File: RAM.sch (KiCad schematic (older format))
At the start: 19 parts, among them U1 xc7a50tftg256, U14 W9751G6KB

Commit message: using BOMs AWAY to create BOM
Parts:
- C126, C129: MFR (none) -> Murata; MPN (none) -> GRM21BR61A106KE19L
- C127, C128, C130, C131, C132, C133: MFR (none) -> Murata; MPN (none) -> GRM188R71C104KA01D
- C136: MFR (none) -> Murata Manufacturing Co Ltd; MPN (none) -> GRM32ER70J476ME20L
- C137, C138: MFR (none) -> Murata; MPN (none) -> GRM21BR61A475KA73L
- C139, C140, C141, C142: MFR (none) -> Murata; MPN (none) -> GRM188R71C474KA88D
- R56, R57: MFR (none) -> Vishay Dale; MPN (none) -> CRCW040210K0FKED
- U1: MFR (none) -> Xilinx; MPN (none) -> XC7A50T-1FTG256C
- U14: MFR (none) -> Winbond Electronics Corp; MPN (none) -> W9751G6KB-25

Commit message: just added NOTE field to BOMS AWAY
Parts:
- C126, C129: SPN (none) -> 490-1709-1-ND; SPR (none) -> Digikey
- C127, C128, C130, C131, C132, C133: SPN (none) -> 490-1532-1-ND; SPR (none) -> Digikey
- C136: SPN (none) -> 490-6542-1-ND; SPR (none) -> Digikey
- C137, C138: SPN (none) -> 490-9750-1-ND; SPR (none) -> Digikey
- C139, C140, C141, C142: SPN (none) -> 490-3295-1-ND; SPR (none) -> Digikey
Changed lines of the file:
@@
 F 4 "Murata" H 0 0 50 0001 C CNN "MFR"
 F 5 "GRM188R71C104KA01D" H 0 0 50 0001 C CNN "MPN"
-F 6 "" H 0 0 50 0001 C CNN "SPR"
-F 7 "" H 0 0 50 0001 C CNN "SPN"
+F 6 "Digikey" H 0 0 50 0001 C CNN "SPR"
+F 7 "490-1532-1-ND" H 0 0 50 0001 C CNN "SPN"
 F 8 "" H 0 0 50 0001 C CNN "SPURL"
 	1    1000 4550
@@
 F 4 "Murata" H 0 0 50 0001 C CNN "MFR"
 F 5 "GRM188R71C104KA01D" H 0 0 50 0001 C CNN "MPN"
-F 6 "" H 0 0 50 0001 C CNN "SPR"
-F 7 "" H 0 0 50 0001 C CNN "SPN"
+F 6 "Digikey" H 0 0 50 0001 C CNN "SPR"
+F 7 "490-1532-1-ND" H 0 0 50 0001 C CNN "SPN"
 F 8 "" H 0 0 50 0001 C CNN "SPURL"
 	1    1000 5050
@@
 F 4 "Murata" H 0 0 50 0001 C CNN "MFR"
 F 5 "GRM188R71C104KA01D" H 0 0 50 0001 C CNN "MPN"
-F 6 "" H 0 0 50 0001 C CNN "SPR"
-F 7 "" H 0 0 50 0001 C CNN "SPN"
+F 6 "Digikey" H 0 0 50 0001 C CNN "SPR"
+F 7 "490-1532-1-ND" H 0 0 50 0001 C CNN "SPN"
 F 8 "" H 0 0 50 0001 C CNN "SPURL"
 	1    1600 4550
@@
 F 4 "Murata" H 0 0 50 0001 C CNN "MFR"
 F 5 "GRM188R71C104KA01D" H 0 0 50 0001 C CNN "MPN"
-F 6 "" H 0 0 50 0001 C CNN "SPR"
-F 7 "" H 0 0 50 0001 C CNN "SPN"
+F 6 "Digikey" H 0 0 50 0001 C CNN "SPR"
+F 7 "490-1532-1-ND" H 0 0 50 0001 C CNN "SPN"
 F 8 "" H 0 0 50 0001 C CNN "SPURL"
 	1    1600 5050
@@
 F 4 "Murata" H 0 0 50 0001 C CNN "MFR"
 F 5 "GRM188R71C104KA01D" H 0 0 50 0001 C CNN "MPN"
-F 6 "" H 0 0 50 0001 C CNN "SPR"
-F 7 "" H 0 0 50 0001 C CNN "SPN"
+F 6 "Digikey" H 0 0 50 0001 C CNN "SPR"
+F 7 "490-1532-1-ND" H 0 0 50 0001 C CNN "SPN"
 F 8 "" H 0 0 50 0001 C CNN "SPURL"
 	1    1500 6000
@@
 F 4 "Murata" H 0 0 50 0001 C CNN "MFR"
 F 5 "GRM188R71C104KA01D" H 0 0 50 0001 C CNN "MPN"
-F 6 "" H 0 0 50 0001 C CNN "SPR"
-F 7 "" H 0 0 50 0001 C CNN "SPN"
+F 6 "Digikey" H 0 0 50 0001 C CNN "SPR"
+F 7 "490-1532-1-ND" H 0 0 50 0001 C CNN "SPN"
 F 8 "" H 0 0 50 0001 C CNN "SPURL"
 	1    1250 6000
@@
 F 4 "Murata" H 0 0 50 0001 C CNN "MFR"
 F 5 "GRM21BR61A106KE19L" H 0 0 50 0001 C CNN "MPN"
-F 6 "" H 0 0 50 0001 C CNN "SPR"
-F 7 "" H 0 0 50 0001 C CNN "SPN"
+F 6 "Digikey" H 0 0 50 0001 C CNN "SPR"
+F 7 "490-1709-1-ND" H 0 0 50 0001 C CNN "SPN"
 F 8 "" H 0 0 50 0001 C CNN "SPURL"
 	1    1000 6000
@@
 F 4 "Murata" H 0 0 50 0001 C CNN "MFR"
 F 5 "GRM21BR61A106KE19L" H 0 0 50 0001 C CNN "MPN"
-F 6 "" H 0 0 50 0001 C CNN "SPR"
-F 7 "" H 0 0 50 0001 C CNN "SPN"
+F 6 "Digikey" H 0 0 50 0001 C CNN "SPR"
+F 7 "490-1709-1-ND" H 0 0 50 0001 C CNN "SPN"
 F 8 "" H 0 0 50 0001 C CNN "SPURL"
 	1    750  6000
@@
 F 4 "Murata Manufacturing Co Ltd" H 0 0 50 0001 C CNN "MFR"
 F 5 "GRM32ER70J476ME20L" H 0 0 50 0001 C CNN "MPN"
-F 6 "" H 0 0 50 0001 C CNN "SPR"
-F 7 "" H 0 0 50 0001 C CNN "SPN"
+F 6 "Digikey" H 0 0 50 0001 C CNN "SPR"
+F 7 "490-6542-1-ND" H 0 0 50 0001 C CNN "SPN"
 F 8 "" H 0 0 50 0001 C CNN "SPURL"
 	1    6900 5950
@@
 F 4 "Murata" H 0 0 50 0001 C CNN "MFR"
 F 5 "GRM21BR61A475KA73L" H 0 0 50 0001 C CNN "MPN"
-F 6 "" H 0 0 50 0001 C CNN "SPR"
-F 7 "" H 0 0 50 0001 C CNN "SPN"
+F 6 "Digikey" H 0 0 50 0001 C CNN "SPR"
+F 7 "490-9750-1-ND" H 0 0 50 0001 C CNN "SPN"
 F 8 "" H 0 0 50 0001 C CNN "SPURL"
 	1    7150 5950
@@
 F 4 "Murata" H 0 0 50 0001 C CNN "MFR"
 F 5 "GRM21BR61A475KA73L" H 0 0 50 0001 C CNN "MPN"
-F 6 "" H 0 0 50 0001 C CNN "SPR"
-F 7 "" H 0 0 50 0001 C CNN "SPN"
+F 6 "Digikey" H 0 0 50 0001 C CNN "SPR"
+F 7 "490-9750-1-ND" H 0 0 50 0001 C CNN "SPN"
 F 8 "" H 0 0 50 0001 C CNN "SPURL"
 	1    7400 5950
@@
 F 4 "Murata" H 0 0 50 0001 C CNN "MFR"
 F 5 "GRM188R71C474KA88D" H 0 0 50 0001 C CNN "MPN"
-F 6 "" H 0 0 50 0001 C CNN "SPR"
-F 7 "" H 0 0 50 0001 C CNN "SPN"
+F 6 "Digikey" H 0 0 50 0001 C CNN "SPR"
+F 7 "490-3295-1-ND" H 0 0 50 0001 C CNN "SPN"
 F 8 "" H 0 0 50 0001 C CNN "SPURL"
 	1    7650 5950
@@
 F 4 "Murata" H 0 0 50 0001 C CNN "MFR"
 F 5 "GRM188R71C474KA88D" H 0 0 50 0001 C CNN "MPN"
-F 6 "" H 0 0 50 0001 C CNN "SPR"
-F 7 "" H 0 0 50 0001 C CNN "SPN"
+F 6 "Digikey" H 0 0 50 0001 C CNN "SPR"
+F 7 "490-3295-1-ND" H 0 0 50 0001 C CNN "SPN"
 F 8 "" H 0 0 50 0001 C CNN "SPURL"
 	1    7900 5950
@@
 F 4 "Murata" H 0 0 50 0001 C CNN "MFR"
 F 5 "GRM188R71C474KA88D" H 0 0 50 0001 C CNN "MPN"
-F 6 "" H 0 0 50 0001 C CNN "SPR"
-F 7 "" H 0 0 50 0001 C CNN "SPN"
+F 6 "Digikey" H 0 0 50 0001 C CNN "SPR"
+F 7 "490-3295-1-ND" H 0 0 50 0001 C CNN "SPN"
 F 8 "" H 0 0 50 0001 C CNN "SPURL"
 	1    8150 5950
@@
 F 4 "Murata" H 0 0 50 0001 C CNN "MFR"
 F 5 "GRM188R71C474KA88D" H 0 0 50 0001 C CNN "MPN"
-F 6 "" H 0 0 50 0001 C CNN "SPR"
-F 7 "" H 0 0 50 0001 C CNN "SPN"
+F 6 "Digikey" H 0 0 50 0001 C CNN "SPR"
+F 7 "490-3295-1-ND" H 0 0 50 0001 C CNN "SPN"
 F 8 "" H 0 0 50 0001 C CNN "SPURL"
 	1    8400 5950

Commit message: Complete BOM. all resistors now 0402
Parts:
- R56, R57: MFR Vishay Dale -> Yageo; MPN CRCW040210K0FKED -> RC0402FR-0710KL; SPN (none) -> 311-10.0KLRTR-ND; SPR (none) -> Digikey
- U1: SPN (none) -> 122-1916-ND; SPR (none) -> Digikey
- U14: SPN (none) -> W9751G6KB-25-ND; SPR (none) -> Digikey

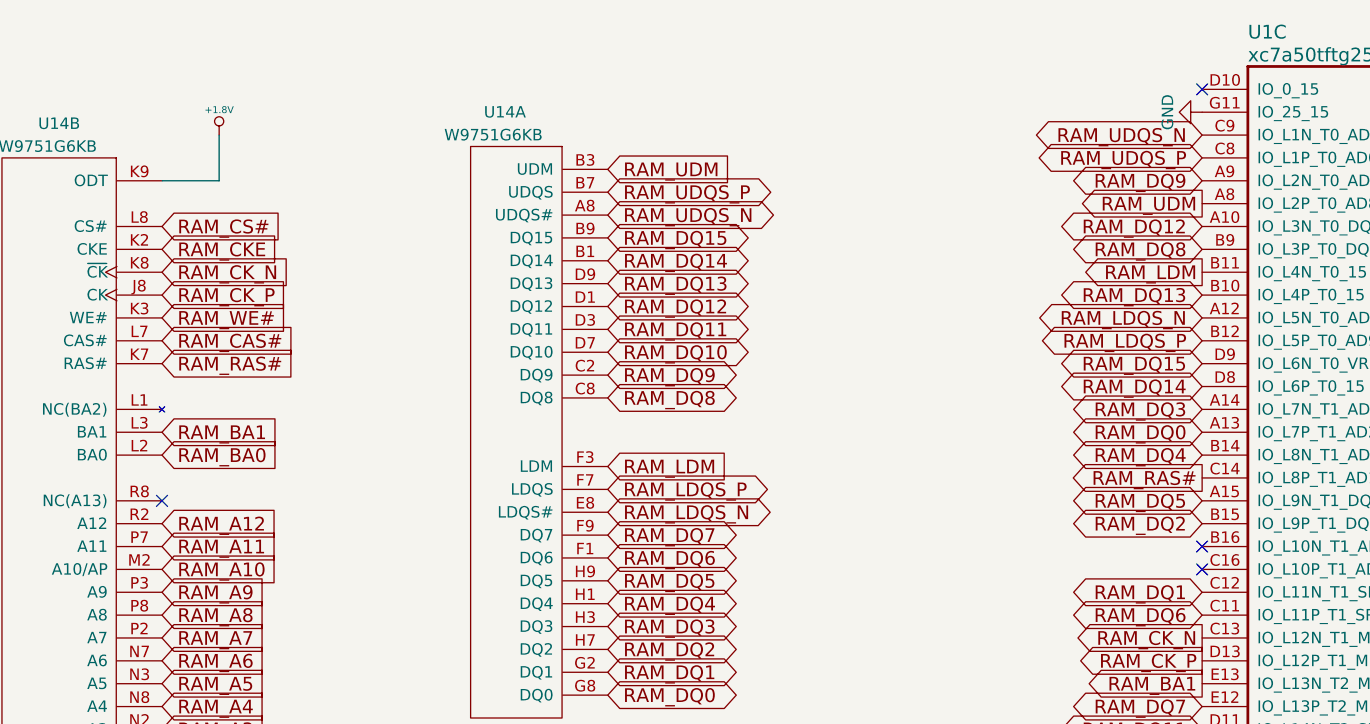
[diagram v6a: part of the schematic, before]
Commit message: attached RAM_ODT signal
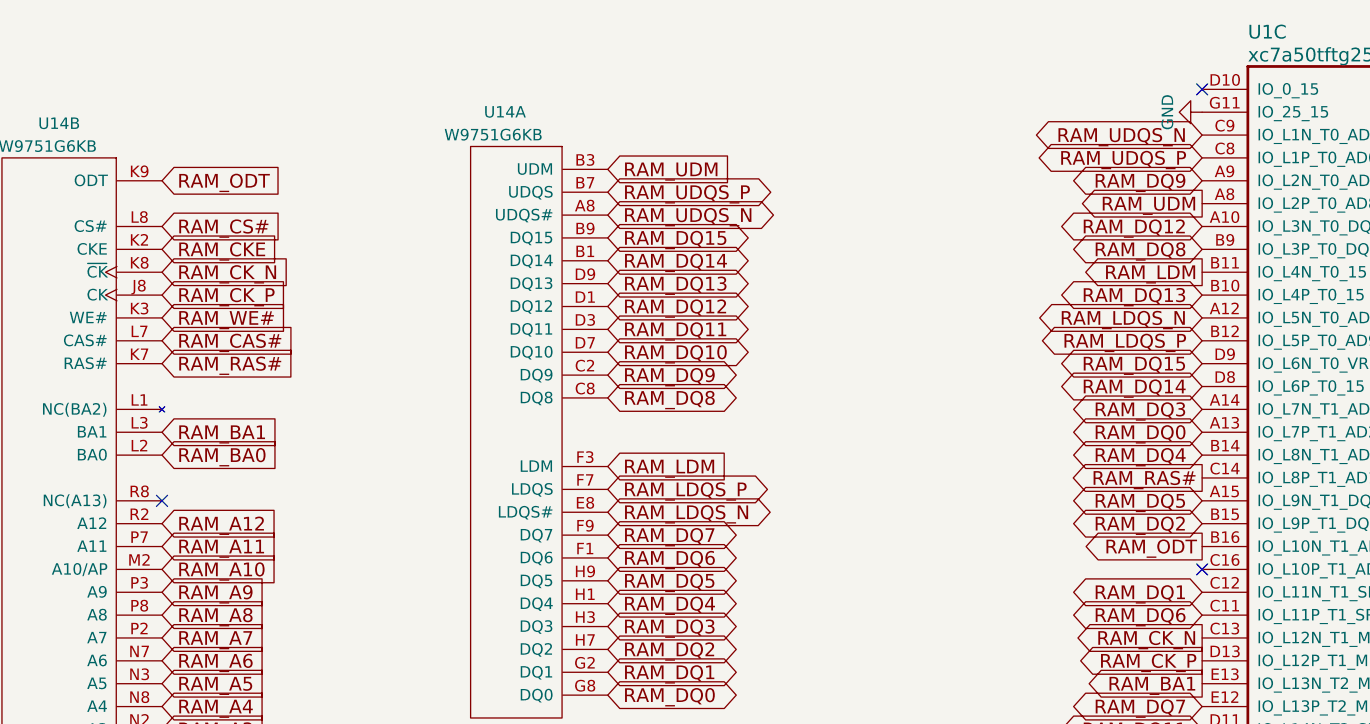
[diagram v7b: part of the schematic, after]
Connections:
- net +1.8V: no longer U14.K9 (ODT)
- net RAM_ODT: now reaches U1.B16 (IO_L10N_T1_AD11N_15)
- net RAM_ODT: now also U14.K9 (ODT)
- no-connect marks 6 -> 5
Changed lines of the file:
@@
-$EndComp
-$Comp
-L +1.8V #PWR0213
-U 1 1 58828F8D
-P 4850 1250
-F 0 "#PWR0213" H 4850 1390 20  0001 C CNN
-F 1 "+1.8V" H 4850 1360 30  0000 C CNN
-F 2 "" H 4850 1250 60  0001 C CNN
-F 3 "" H 4850 1250 60  0001 C CNN
-	1    4850 1250
-	1    0    0    -1
 $EndComp
 $Comp
@@
 	2250 6900 2050 6900
 Wire Wire Line
-	4850 1250 4850 1450
-Wire Wire Line
-	4850 1450 4600 1450
-Wire Wire Line
 	2050 7000 2050 5250
 Wire Wire Line
@@
 NoConn ~ 9150 4950
 NoConn ~ 4600 2850
-NoConn ~ 9150 3050
 NoConn ~ 9150 3150
 NoConn ~ 9150 1050
+Text GLabel 4600 1450 2    60   Input ~ 0
+RAM_ODT
+Text GLabel 9150 3050 0    60   Output ~ 0
+RAM_ODT
 $EndSCHEMATC

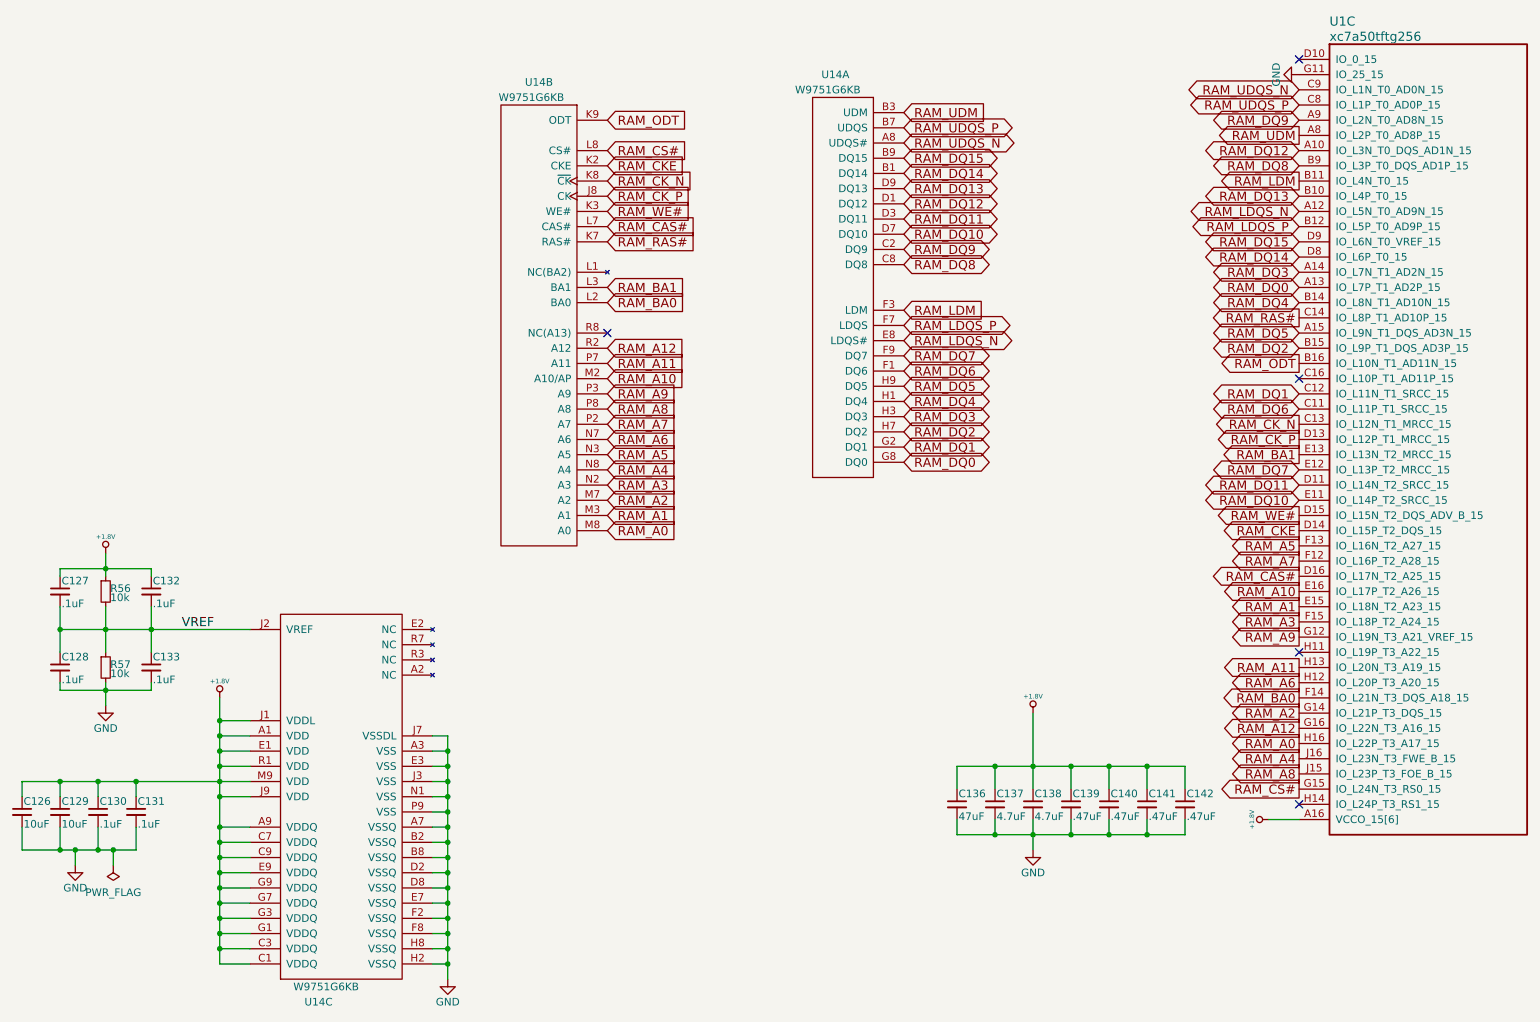
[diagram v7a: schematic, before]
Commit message: about to sed replace all grounds with GND
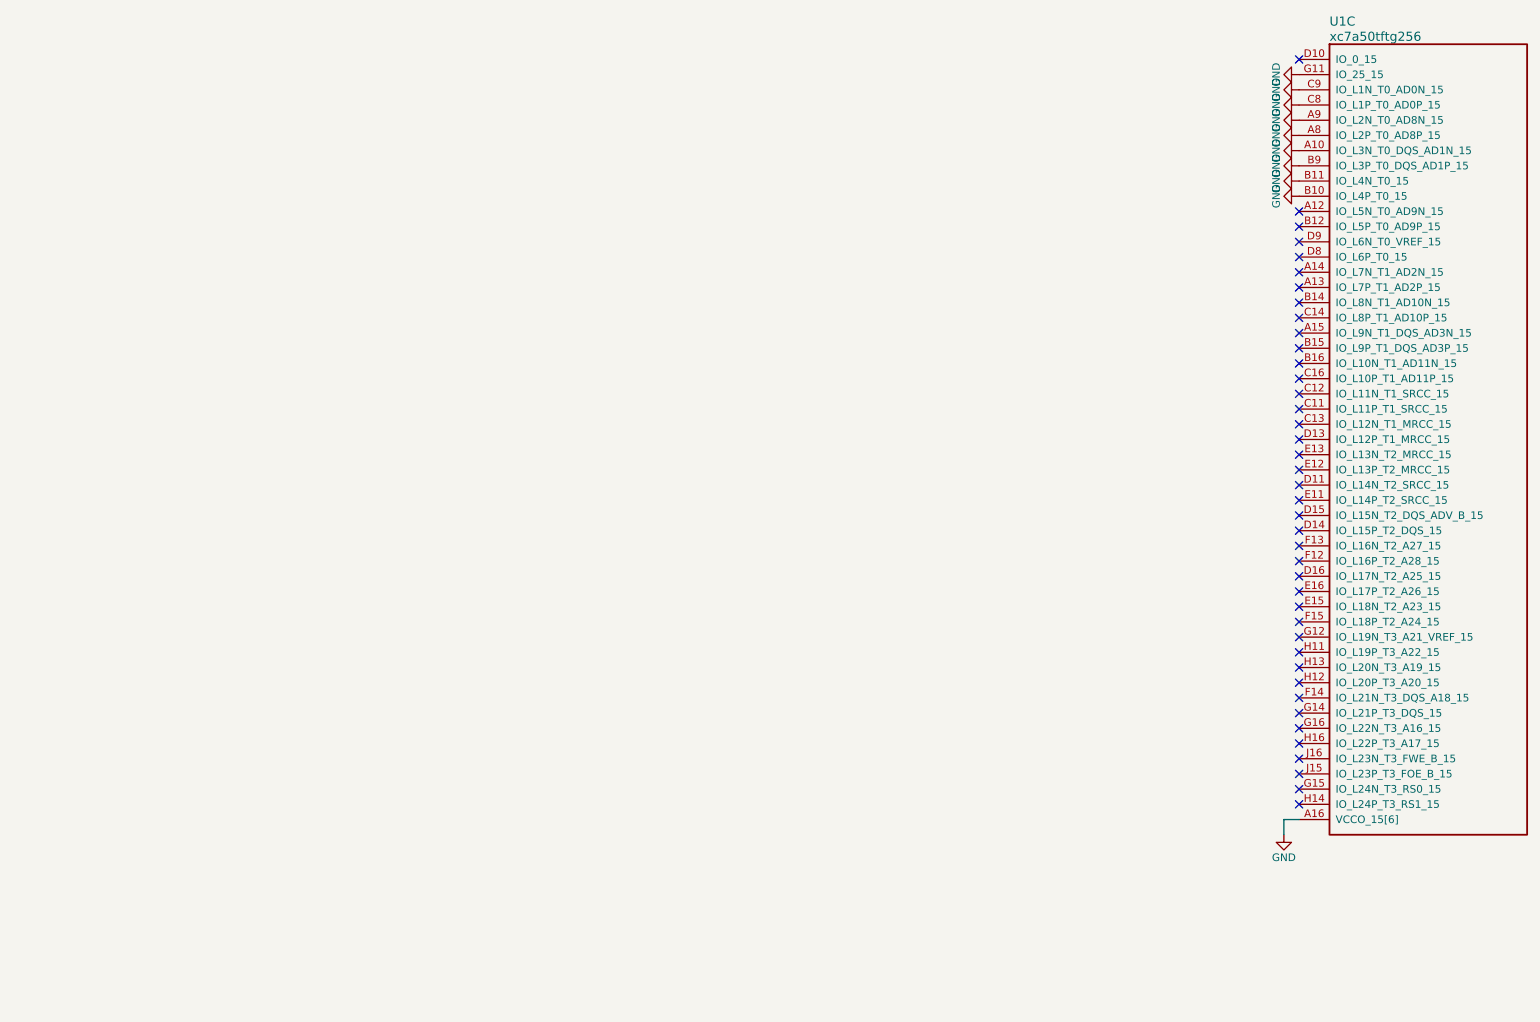
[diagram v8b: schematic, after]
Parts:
- removed C126, C129: 10uF, Capacitors_SMD:C_0805, symbol C_Small
- removed C127, C128, C130, C131, C132, C133: .1uF, Capacitors_SMD:C_0603, symbol C_Small
- removed C136: 47uF, Capacitors_SMD:C_1210, symbol C_Small
- removed C137, C138: 4.7uF, Capacitors_SMD:C_0805, symbol C_Small
- removed C139, C140, C141, C142: .47uF, Capacitors_SMD:C_0603, symbol C_Small
- removed R56, R57: 10k, Resistors_SMD:R_0402, symbol R_Small
- removed U14: W9751G6KB, DFTcustom:WBGA-84, symbol W9751G6KB
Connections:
- net +1.8V is gone; now on net GND: U1.A16 (VCCO_15[6]), U1.B13 (VCCO_15[6]), U1.C10 (VCCO_15[6]), U1.E14 (VCCO_15[6]), U1.H15 (VCCO_15[6]), U1.J12 (VCCO_15[6])
- net RAM_DQ12 is gone; now on net GND: U1.A10 (IO_L3N_T0_DQS_AD1N_15)
- net RAM_DQ13 is gone; now on net GND: U1.B10 (IO_L4P_T0_15)
- net RAM_DQ8 is gone; now on net GND: U1.B9 (IO_L3P_T0_DQS_AD1P_15)
- net RAM_DQ9 is gone; now on net GND: U1.A9 (IO_L2N_T0_AD8N_15)
- net RAM_LDM is gone; now on net GND: U1.B11 (IO_L4N_T0_15)
- net RAM_UDM is gone; now on net GND: U1.A8 (IO_L2P_T0_AD8P_15)
- net RAM_UDQS_N is gone; now on net GND: U1.C9 (IO_L1N_T0_AD0N_15)
- net RAM_UDQS_P is gone; now on net GND: U1.C8 (IO_L1P_T0_AD0P_15)
- net RAM_A0: no longer names the net of U1.H16 (IO_L22P_T3_A17_15)
- net RAM_A1: no longer names the net of U1.E15 (IO_L18N_T2_A23_15)
- net RAM_A10: no longer names the net of U1.E16 (IO_L17P_T2_A26_15)
- net RAM_A11: no longer names the net of U1.H13 (IO_L20N_T3_A19_15)
- net RAM_A12: no longer names the net of U1.G16 (IO_L22N_T3_A16_15)
- net RAM_A2: no longer names the net of U1.G14 (IO_L21P_T3_DQS_15)
- net RAM_A3: no longer names the net of U1.F15 (IO_L18P_T2_A24_15)
- net RAM_A4: no longer names the net of U1.J16 (IO_L23N_T3_FWE_B_15)
- net RAM_A5: no longer names the net of U1.F13 (IO_L16N_T2_A27_15)
- net RAM_A6: no longer names the net of U1.H12 (IO_L20P_T3_A20_15)
- net RAM_A7: no longer names the net of U1.F12 (IO_L16P_T2_A28_15)
- net RAM_A8: no longer names the net of U1.J15 (IO_L23P_T3_FOE_B_15)
- net RAM_A9: no longer names the net of U1.G12 (IO_L19N_T3_A21_VREF_15)
- net RAM_BA0: no longer names the net of U1.F14 (IO_L21N_T3_DQS_A18_15)
- net RAM_BA1: no longer names the net of U1.E13 (IO_L13N_T2_MRCC_15)
- net RAM_CAS#: no longer names the net of U1.D16 (IO_L17N_T2_A25_15)
- net RAM_CKE: no longer names the net of U1.D14 (IO_L15P_T2_DQS_15)
- net RAM_CK_N: no longer names the net of U1.C13 (IO_L12N_T1_MRCC_15)
- net RAM_CK_P: no longer names the net of U1.D13 (IO_L12P_T1_MRCC_15)
- net RAM_CS#: no longer names the net of U1.G15 (IO_L24N_T3_RS0_15)
- net RAM_DQ0: no longer names the net of U1.A13 (IO_L7P_T1_AD2P_15)
- net RAM_DQ1: no longer names the net of U1.C12 (IO_L11N_T1_SRCC_15)
- net RAM_DQ10: no longer names the net of U1.E11 (IO_L14P_T2_SRCC_15)
- net RAM_DQ11: no longer names the net of U1.D11 (IO_L14N_T2_SRCC_15)
- net RAM_DQ14: no longer names the net of U1.D8 (IO_L6P_T0_15)
- net RAM_DQ15: no longer names the net of U1.D9 (IO_L6N_T0_VREF_15)
- net RAM_DQ2: no longer names the net of U1.B15 (IO_L9P_T1_DQS_AD3P_15)
- net RAM_DQ3: no longer names the net of U1.A14 (IO_L7N_T1_AD2N_15)
- net RAM_DQ4: no longer names the net of U1.B14 (IO_L8N_T1_AD10N_15)
- net RAM_DQ5: no longer names the net of U1.A15 (IO_L9N_T1_DQS_AD3N_15)
- net RAM_DQ6: no longer names the net of U1.C11 (IO_L11P_T1_SRCC_15)
- net RAM_DQ7: no longer names the net of U1.E12 (IO_L13P_T2_MRCC_15)
- net RAM_LDQS_N: no longer names the net of U1.A12 (IO_L5N_T0_AD9N_15)
- net RAM_LDQS_P: no longer names the net of U1.B12 (IO_L5P_T0_AD9P_15)
- net RAM_ODT: no longer names the net of U1.B16 (IO_L10N_T1_AD11N_15)
- net RAM_RAS#: no longer names the net of U1.C14 (IO_L8P_T1_AD10P_15)
- net RAM_WE#: no longer names the net of U1.D15 (IO_L15N_T2_DQS_ADV_B_15)
- no-connect marks 5 -> 41
